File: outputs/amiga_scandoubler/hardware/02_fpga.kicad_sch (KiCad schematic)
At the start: 23 parts, among them J4 JTAG 2x05 2.54mm, U2 GW1N-LV4QN88C6/I5

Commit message: Issue 9: sync design documents with the v0.31 U2 pin assignment
- Use the board's U2 pad nets (= amiga_board_top.cst, v031dac) as the reference.
- Rename the 57 U2 pin labels in 02_fpga.kicad_sch.
- Update the netlist, circuit_manifest, fpga_pin_assignment, board_port_map and sync_out_progress (H/V_OUT_RAW now on pins 14/13).
- Checks: a netlist exported from the schematic matches the board on all 587 nodes, and all cst ports exist in the RTL top.
- audit_sync_in_k7.py now passes with no failures.

Co-Authored-By: Claude Opus 5.5 <noreply@anthropic.com>
Claude-Session: https://claude.ai/code/session_019f929sAJ7LRnJRRFvA6g9F
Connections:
- net ADC_B0: now also U2.76 (IOT31B); no longer U2.85 (IOT4B)
- net ADC_B1: now also U2.77 (IOT30B); no longer U2.86 (IOT4A)
- net ADC_B2: now also U2.79 (IOT12A); no longer U2.48 (IOR17B)
- net ADC_B3: now also U2.80 (IOT9A); no longer U2.49 (IOR17A)
- net ADC_B4: now also U2.81 (IOT6B); no longer U2.50 (IOR15B)
- net ADC_B5: now also U2.82 (IOT6A); no longer U2.51 (IOR11B/GCLKC_3)
- net ADC_B6: now also U2.83 (IOT5B); no longer U2.52 (IOR11A/GCLKT_3)
- net ADC_B7: now also U2.84 (IOT5A); no longer U2.53 (IOR10J/DOUT/WE_N)
- net ADC_G0: now also U2.68 (IOT37B); no longer U2.76 (IOT31B)
- net ADC_G1: now also U2.69 (IOT37A); no longer U2.77 (IOT30B)
- net ADC_G2: now also U2.70 (IOT36B); no longer U2.79 (IOT12A)
- net ADC_G3: now also U2.71 (IOT36A); no longer U2.80 (IOT9A)
- net ADC_G4: now also U2.72 (IOT35B); no longer U2.81 (IOT6B)
- net ADC_G5: now also U2.73 (IOT35A); no longer U2.82 (IOT6A)
- net ADC_G6: now also U2.74 (IOT33B); no longer U2.83 (IOT5B)
- net ADC_G7: now also U2.75 (IOT32B); no longer U2.84 (IOT5A)
- net ADC_HS: now also U2.85 (IOT4B); no longer U2.54 (IOR10I/DIN/CLKHOLD_N)
- net ADC_PWDN: now also U2.61 (IOR10B/MO/D6); no longer U2.57 (IOR10E/FASTRD_N/D3)
- net ADC_R0: now also U2.48 (IOR17B); no longer U2.68 (IOT37B)
- net ADC_R1: now also U2.49 (IOR17A); no longer U2.69 (IOT37A)
- net ADC_R2: now also U2.50 (IOR15B); no longer U2.70 (IOT36B)
- net ADC_R3: now also U2.51 (IOR11B/GCLKC_3); no longer U2.71 (IOT36A)
- net ADC_R4: now also U2.52 (IOR11A/GCLKT_3); no longer U2.72 (IOT35B)
- net ADC_R5: now also U2.53 (IOR10J/DOUT/WE_N); no longer U2.73 (IOT35A)
- net ADC_R6: now also U2.54 (IOR10I/DIN/CLKHOLD_N); no longer U2.74 (IOT33B)
- net ADC_R7: now also U2.55 (IOR10H/SSPI_CS_N/D0); no longer U2.75 (IOT32B)
- net ADC_RESET_N: now also U2.60 (IOR10C/MCS_N/D5); no longer U2.15 (IOL17A)
- net ADC_VS: now also U2.86 (IOT4A); no longer U2.55 (IOR10H/SSPI_CS_N/D0)
- net DAC_B0: now also U2.26 (IOB6B); no longer U2.37 (IOB26B)
- net DAC_B1: now also U2.25 (IOB6A); no longer U2.38 (IOB27B)
- net DAC_B2: now also U2.20 (IOB4B); no longer U2.39 (IOB28A)
- net DAC_B3: now also U2.19 (IOB4A); no longer U2.40 (IOB28B)
- net DAC_B4: now also U2.18 (IOB2B); no longer U2.41 (IOB30A)
- net DAC_B5: now also U2.17 (IOB2A); no longer U2.42 (IOB30B)
- net DAC_B6: now also U2.16 (IOL17B); no longer U2.47 (IOB36B)
- net DAC_B7: now also U2.15 (IOL17A); no longer U2.3 (IOL2A)
- net DAC_BLANK_N: now also U2.27 (IOB8A); no longer U2.59 (IOR10D/MCLK/D4)
- net DAC_CLK_RAW: now also U2.3 (IOL2A); no longer U2.16 (IOL17B)
- net DAC_G0: now also U2.35 (IOB20A/GCLKT_4); no longer U2.29 (IOB10A)
- net DAC_G1: now also U2.34 (IOB15A); no longer U2.30 (IOB10B)
- net DAC_G2: now also U2.33 (IOB14A); no longer U2.31 (IOB12A)
- net DAC_G4: now also U2.31 (IOB12A); no longer U2.33 (IOB14A)
- net DAC_G5: now also U2.30 (IOB10B); no longer U2.34 (IOB15A)
- net DAC_G6: now also U2.29 (IOB10A); no longer U2.35 (IOB20A/GCLKT_4)
- net DAC_G7: now also U2.28 (IOB8B); no longer U2.36 (IOB20B/GCLKC_4)
- net DAC_R0: now also U2.47 (IOB36B); no longer U2.17 (IOB2A)
- net DAC_R1: now also U2.42 (IOB30B); no longer U2.18 (IOB2B)
- net DAC_R2: now also U2.41 (IOB30A); no longer U2.19 (IOB4A)
- net DAC_R3: now also U2.40 (IOB28B); no longer U2.20 (IOB4B)
- net DAC_R4: now also U2.39 (IOB28A); no longer U2.25 (IOB6A)
- net DAC_R5: now also U2.38 (IOB27B); no longer U2.26 (IOB6B)
- net DAC_R6: now also U2.37 (IOB26B); no longer U2.27 (IOB8A)
- net DAC_R7: now also U2.36 (IOB20B/GCLKC_4); no longer U2.28 (IOB8B)
- net H_OUT_RAW: now also U2.14 (IOL15B); no longer U2.60 (IOR10C/MCS_N/D5)
- net I2C_SCL: now also U2.59 (IOR10D/MCLK/D4); no longer U2.13 (IOL15A)
- net I2C_SDA: now also U2.57 (IOR10E/FASTRD_N/D3); no longer U2.14 (IOL15B)
- net V_OUT_RAW: now also U2.13 (IOL15A); no longer U2.61 (IOR10B/MO/D6)

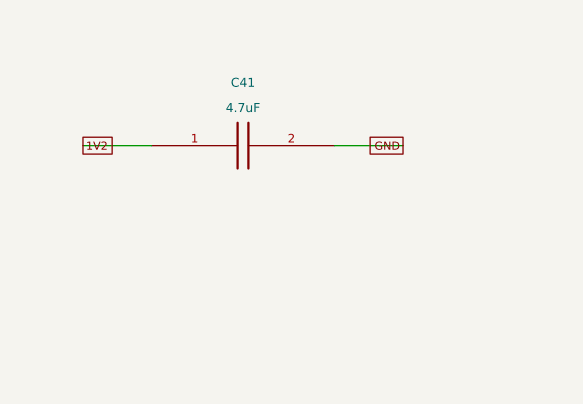
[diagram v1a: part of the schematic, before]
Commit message: Review fixes: decaps for U2 VCCO pins 12/23; move In2 lines off GIN_1
- #1: Add C70/C71 (100nF 0402) at 1.5 / 1.1 mm from U2 pins 12/23. Schematic, netlist and manifest updated; the schematic export matches the board on 591 nodes.
- #2: Re-draw the In2 ADC_3V3A/ADC_1V9A links so they cross GIN_1 instead of running under it (gap 4.9 -> 4.5 mm).
- #3: Stitching vias dropped. With In1 as the only GND plane they connect to nothing. Decaps near the REF_27M vias remain proposed.
- DRC errors 0, unconnected 0. The audit passes; its part/pad counts are updated to 137/596.

Co-Authored-By: Claude Opus 5.5 <noreply@anthropic.com>
Claude-Session: https://claude.ai/code/session_019f929sAJ7LRnJRRFvA6g9F
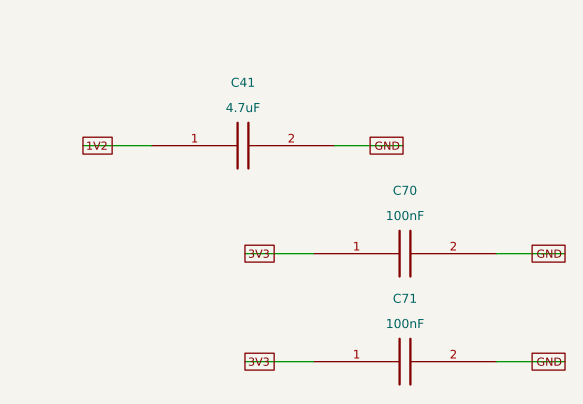
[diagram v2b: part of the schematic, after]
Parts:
- added C70, C71: 100nF, Capacitor_SMD:C_0402_1005Metric, symbol Amiga:C
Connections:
- net 3V3: now also C70.1, C71.1
- net GND: now also C70.2, C71.2
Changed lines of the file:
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@@
+(pin "2")
+)
+(wire (pts (xy 357.84 256) (xy 350.22 256)) (stroke (width 0) (type default)))
+(global_label "3V3" (shape passive) (at 350.22 256 0) (effects (font (size 0.9 0.9)) (justify left)))
+(wire (pts (xy 378.16 256) (xy 385.78 256)) (stroke (width 0) (type default)))
+(global_label "GND" (shape passive) (at 385.78 256 180) (effects (font (size 0.9 0.9)) (justify right)))
+(symbol (lib_id "Amiga:C") (at 368 256 0) (unit 1) (in_bom yes) (on_board yes)
+(property "Reference" "C70" (id 0) (at 368 249 0) (effects (font (size 1.0 1.0)) ))
+(property "Value" "100nF" (id 1) (at 368 251.8 0) (effects (font (size 1.0 1.0)) ))
+(property "Footprint" "Capacitor_SMD:C_0402_1005Metric" (id 2) (at 368 251.8 0) (effects (font (size 1.0 1.0)) hide))
+(property "Datasheet" "" (id 3) (at 368 251.8 0) (effects (font (size 1.0 1.0)) hide))
+(property "MPN" "100nF" (id 4) (at 368 251.8 0) (effects (font (size 1.0 1.0)) hide))
+(property "LCSC" "" (id 5) (at 368 251.8 0) (effects (font (size 1.0 1.0)) hide))
+(pin "1")
+(pin "2")
+)
+(wire (pts (xy 357.84 268) (xy 350.22 268)) (stroke (width 0) (type default)))
+(global_label "3V3" (shape passive) (at 350.22 268 0) (effects (font (size 0.9 0.9)) (justify left)))
+(wire (pts (xy 378.16 268) (xy 385.78 268)) (stroke (width 0) (type default)))
+(global_label "GND" (shape passive) (at 385.78 268 180) (effects (font (size 0.9 0.9)) (justify right)))
+(symbol (lib_id "Amiga:C") (at 368 268 0) (unit 1) (in_bom yes) (on_board yes)
+(property "Reference" "C71" (id 0) (at 368 261 0) (effects (font (size 1.0 1.0)) ))
+(property "Value" "100nF" (id 1) (at 368 263.8 0) (effects (font (size 1.0 1.0)) ))
+(property "Footprint" "Capacitor_SMD:C_0402_1005Metric" (id 2) (at 368 263.8 0) (effects (font (size 1.0 1.0)) hide))
+(property "Datasheet" "" (id 3) (at 368 263.8 0) (effects (font (size 1.0 1.0)) hide))
+(property "MPN" "100nF" (id 4) (at 368 263.8 0) (effects (font (size 1.0 1.0)) hide))
+(property "LCSC" "" (id 5) (at 368 263.8 0) (effects (font (size 1.0 1.0)) hide))
+(pin "1")
 (pin "2")
 )
@@
 (path "/d7285cc1-01a7-52b5-b1b4-a16a6a4410c1/ecfa7323-a425-5fed-9824-71c38a2d27b0/a6f465c4-68e1-5243-a013-80e4dc853064" (reference "C35") (unit 1) (value "100nF") (footprint "Capacitor_SMD:C_0603_1608Metric"))
 (path "/d7285cc1-01a7-52b5-b1b4-a16a6a4410c1/ecfa7323-a425-5fed-9824-71c38a2d27b0/f25a1926-877c-5038-a457-b9606053b4e7" (reference "C36") (unit 1) (value "100nF") (footprint "Capacitor_SMD:C_0603_1608Metric"))
+(path "/d7285cc1-01a7-52b5-b1b4-a16a6a4410c1/ecfa7323-a425-5fed-9824-71c38a2d27b0/a0e1c070-0000-4000-8000-00000000c070" (reference "C70") (unit 1) (value "100nF") (footprint "Capacitor_SMD:C_0402_1005Metric"))
+(path "/d7285cc1-01a7-52b5-b1b4-a16a6a4410c1/ecfa7323-a425-5fed-9824-71c38a2d27b0/a0e1c071-0000-4000-8000-00000000c071" (reference "C71") (unit 1) (value "100nF") (footprint "Capacitor_SMD:C_0402_1005Metric"))
 (path "/d7285cc1-01a7-52b5-b1b4-a16a6a4410c1/ecfa7323-a425-5fed-9824-71c38a2d27b0/67319627-409e-5caa-8b53-fe988aff5722" (reference "C37") (unit 1) (value "100nF") (footprint "Capacitor_SMD:C_0603_1608Metric"))
 (path "/d7285cc1-01a7-52b5-b1b4-a16a6a4410c1/ecfa7323-a425-5fed-9824-71c38a2d27b0/e3e5aa43-c778-574c-beeb-5f578075735f" (reference "C38") (unit 1) (value "100nF") (footprint "Capacitor_SMD:C_0603_1608Metric"))

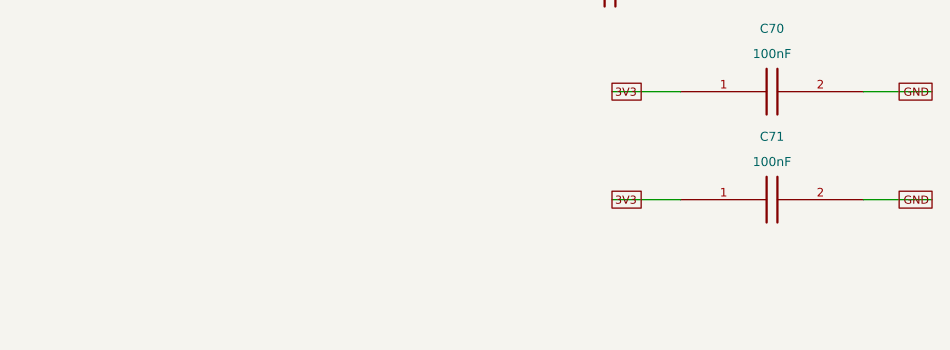
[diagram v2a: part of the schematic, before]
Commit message: Add decaps C72/C73 next to the REF_27M layer-change vias
- Placements found by tools/capvia.py (0402, short stubs to new plane vias, no via-in-pad).
- Via-to-decap distance: 5.2 -> 1.6 mm and 4.3 -> 0.8 mm. The via under U1 (30.4,35.6) has no room and stays at 6.2 mm.
- Schematic (02_fpga), netlist and manifest updated; the schematic export matches the board on 595 nodes.
- DRC errors 0, unconnected 0. The audit passes with 139 parts / 600 pad nets.

Co-Authored-By: Claude Opus 5.5 <noreply@anthropic.com>
Claude-Session: https://claude.ai/code/session_019f929sAJ7LRnJRRFvA6g9F
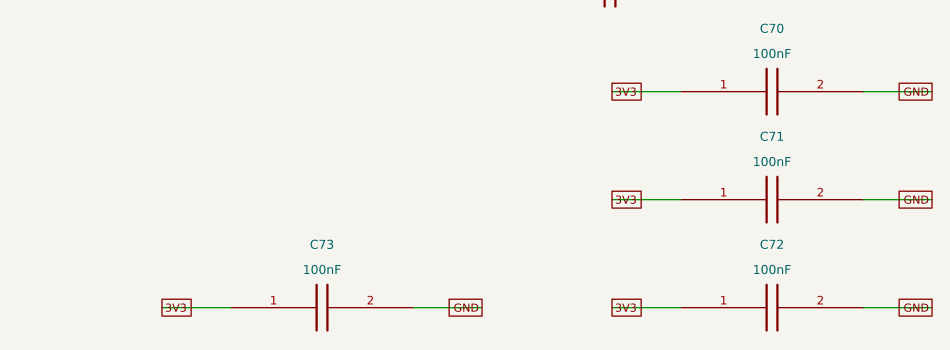
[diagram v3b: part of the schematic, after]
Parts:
- added C72, C73: 100nF, Capacitor_SMD:C_0402_1005Metric, symbol Amiga:C
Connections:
- net 3V3: now also C72.1, C73.1
- net GND: now also C72.2, C73.2
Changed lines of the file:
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@@
+(pin "2")
+)
+(wire (pts (xy 357.84 280) (xy 350.22 280)) (stroke (width 0) (type default)))
+(global_label "3V3" (shape passive) (at 350.22 280 0) (effects (font (size 0.9 0.9)) (justify left)))
+(wire (pts (xy 378.16 280) (xy 385.78 280)) (stroke (width 0) (type default)))
+(global_label "GND" (shape passive) (at 385.78 280 180) (effects (font (size 0.9 0.9)) (justify right)))
+(symbol (lib_id "Amiga:C") (at 368 280 0) (unit 1) (in_bom yes) (on_board yes)
+(property "Reference" "C72" (id 0) (at 368 273 0) (effects (font (size 1.0 1.0)) ))
+(property "Value" "100nF" (id 1) (at 368 275.8 0) (effects (font (size 1.0 1.0)) ))
+(property "Footprint" "Capacitor_SMD:C_0402_1005Metric" (id 2) (at 368 275.8 0) (effects (font (size 1.0 1.0)) hide))
+(property "Datasheet" "" (id 3) (at 368 275.8 0) (effects (font (size 1.0 1.0)) hide))
+(property "MPN" "100nF" (id 4) (at 368 275.8 0) (effects (font (size 1.0 1.0)) hide))
+(property "LCSC" "" (id 5) (at 368 275.8 0) (effects (font (size 1.0 1.0)) hide))
+(pin "1")
+(pin "2")
+)
+(wire (pts (xy 307.84 280) (xy 300.22 280)) (stroke (width 0) (type default)))
+(global_label "3V3" (shape passive) (at 300.22 280 0) (effects (font (size 0.9 0.9)) (justify left)))
+(wire (pts (xy 328.16 280) (xy 335.78 280)) (stroke (width 0) (type default)))
+(global_label "GND" (shape passive) (at 335.78 280 180) (effects (font (size 0.9 0.9)) (justify right)))
+(symbol (lib_id "Amiga:C") (at 318 280 0) (unit 1) (in_bom yes) (on_board yes)
+(property "Reference" "C73" (id 0) (at 318 273 0) (effects (font (size 1.0 1.0)) ))
+(property "Value" "100nF" (id 1) (at 318 275.8 0) (effects (font (size 1.0 1.0)) ))
+(property "Footprint" "Capacitor_SMD:C_0402_1005Metric" (id 2) (at 318 275.8 0) (effects (font (size 1.0 1.0)) hide))
+(property "Datasheet" "" (id 3) (at 318 275.8 0) (effects (font (size 1.0 1.0)) hide))
+(property "MPN" "100nF" (id 4) (at 318 275.8 0) (effects (font (size 1.0 1.0)) hide))
+(property "LCSC" "" (id 5) (at 318 275.8 0) (effects (font (size 1.0 1.0)) hide))
+(pin "1")
 (pin "2")
 )
@@
 (path "/d7285cc1-01a7-52b5-b1b4-a16a6a4410c1/ecfa7323-a425-5fed-9824-71c38a2d27b0/a6f465c4-68e1-5243-a013-80e4dc853064" (reference "C35") (unit 1) (value "100nF") (footprint "Capacitor_SMD:C_0603_1608Metric"))
 (path "/d7285cc1-01a7-52b5-b1b4-a16a6a4410c1/ecfa7323-a425-5fed-9824-71c38a2d27b0/f25a1926-877c-5038-a457-b9606053b4e7" (reference "C36") (unit 1) (value "100nF") (footprint "Capacitor_SMD:C_0603_1608Metric"))
+(path "/d7285cc1-01a7-52b5-b1b4-a16a6a4410c1/ecfa7323-a425-5fed-9824-71c38a2d27b0/a0e1c072-0000-4000-8000-00000000c072" (reference "C72") (unit 1) (value "100nF") (footprint "Capacitor_SMD:C_0402_1005Metric"))
+(path "/d7285cc1-01a7-52b5-b1b4-a16a6a4410c1/ecfa7323-a425-5fed-9824-71c38a2d27b0/a0e1c073-0000-4000-8000-00000000c073" (reference "C73") (unit 1) (value "100nF") (footprint "Capacitor_SMD:C_0402_1005Metric"))
 (path "/d7285cc1-01a7-52b5-b1b4-a16a6a4410c1/ecfa7323-a425-5fed-9824-71c38a2d27b0/a0e1c070-0000-4000-8000-00000000c070" (reference "C70") (unit 1) (value "100nF") (footprint "Capacitor_SMD:C_0402_1005Metric"))
 (path "/d7285cc1-01a7-52b5-b1b4-a16a6a4410c1/ecfa7323-a425-5fed-9824-71c38a2d27b0/a0e1c071-0000-4000-8000-00000000c071" (reference "C71") (unit 1) (value "100nF") (footprint "Capacitor_SMD:C_0402_1005Metric"))

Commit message: Select LCSC parts with live JLCPCB stock/price (135 of 139 parts)
- r11_select.py queries JLCPCB's public component search. It matches package and spec (C/V/dielectric, R/tolerance, 0.1% thin film) and ranks basic > preferred > stock.
- Results are in fab/v030wip/parts_selection.csv/.json. r11_apply.py writes LCSC/MPN into the manifest, schematic symbols and netlist.
- Open items:
  - U1 TVP7002: stock 4.
  - J1/J2 CONEC 33DSMT1-E15SNCT: stock 0.
  - Y1 ECS-3225MVLC-270: stock 4. YXC OT2EL4C4JI-111OLP-27M (C5203549) is a datasheet-checked drop-in candidate.
- Nets unchanged (595 nodes match the board). The audit passes. Nothing ordered.

Co-Authored-By: Claude Opus 5.5 <noreply@anthropic.com>
Claude-Session: https://claude.ai/code/session_019f929sAJ7LRnJRRFvA6g9F
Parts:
- C29, C30, C31, C32, C33, C34, C35, C36, C37, C38, C39: LCSC (none) -> C14663; MPN 100nF -> CC0603KRX7R9BB104
- C40, C41: LCSC (none) -> C1779; MPN 4.7uF -> CL21A475KAQNNNE
- C70, C71, C72, C73: LCSC (none) -> C1525; MPN 100nF -> CL05B104KO5NNNC
- J4: LCSC (none) -> C32713285; MPN JTAG 2x05 2.54mm -> HX PZ2.54-2x5P TP
- R2, R3, R4, R5, R6, R7, R8, R9: LCSC (none) -> C23162; MPN 4.7k -> 0603WAF4701T5E
